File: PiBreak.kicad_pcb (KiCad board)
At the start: 2 copper layers, 56 x 62.9 mm, 317 parts, among them P1 RASPBERRY_PI_P1, P2 CONN_17, P3 CONN_8, P4 CONN_8, P5 CONN_8

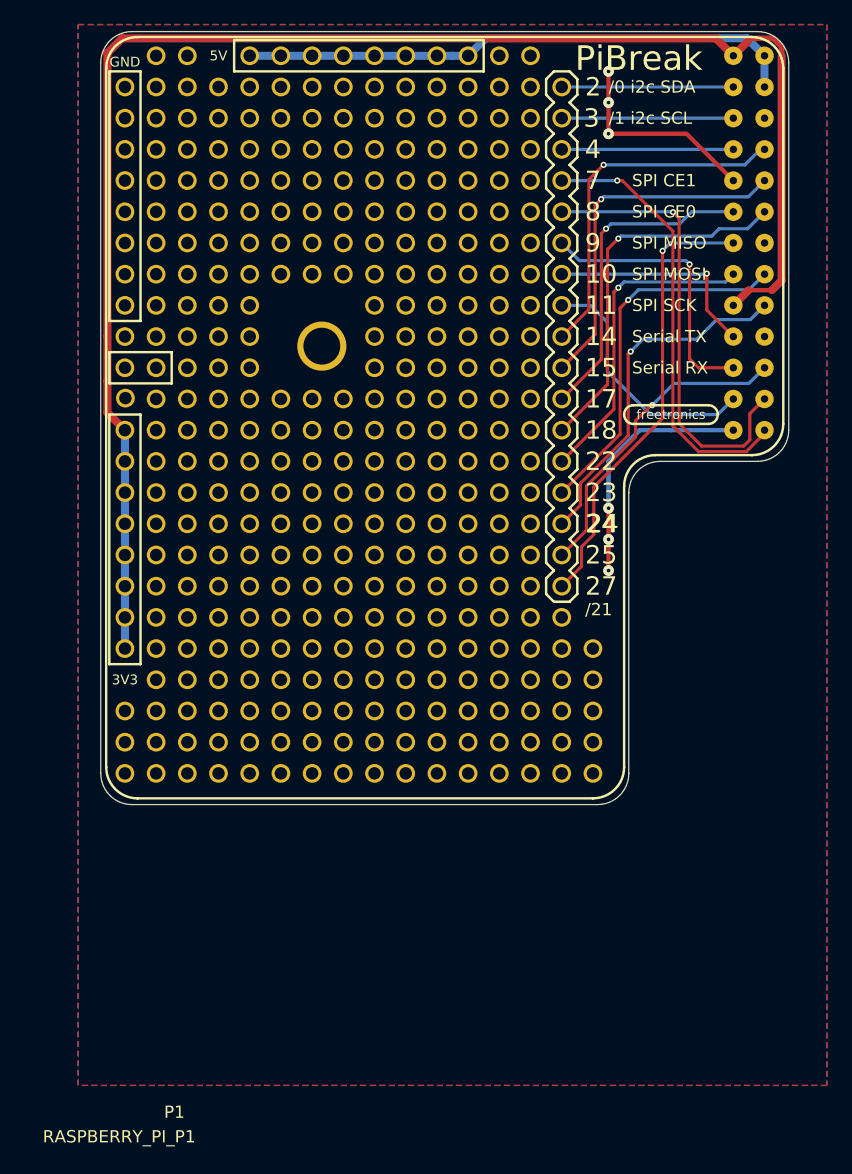
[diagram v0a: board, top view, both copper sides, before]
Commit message: Fix pad size for P1 header (was marginally too small)
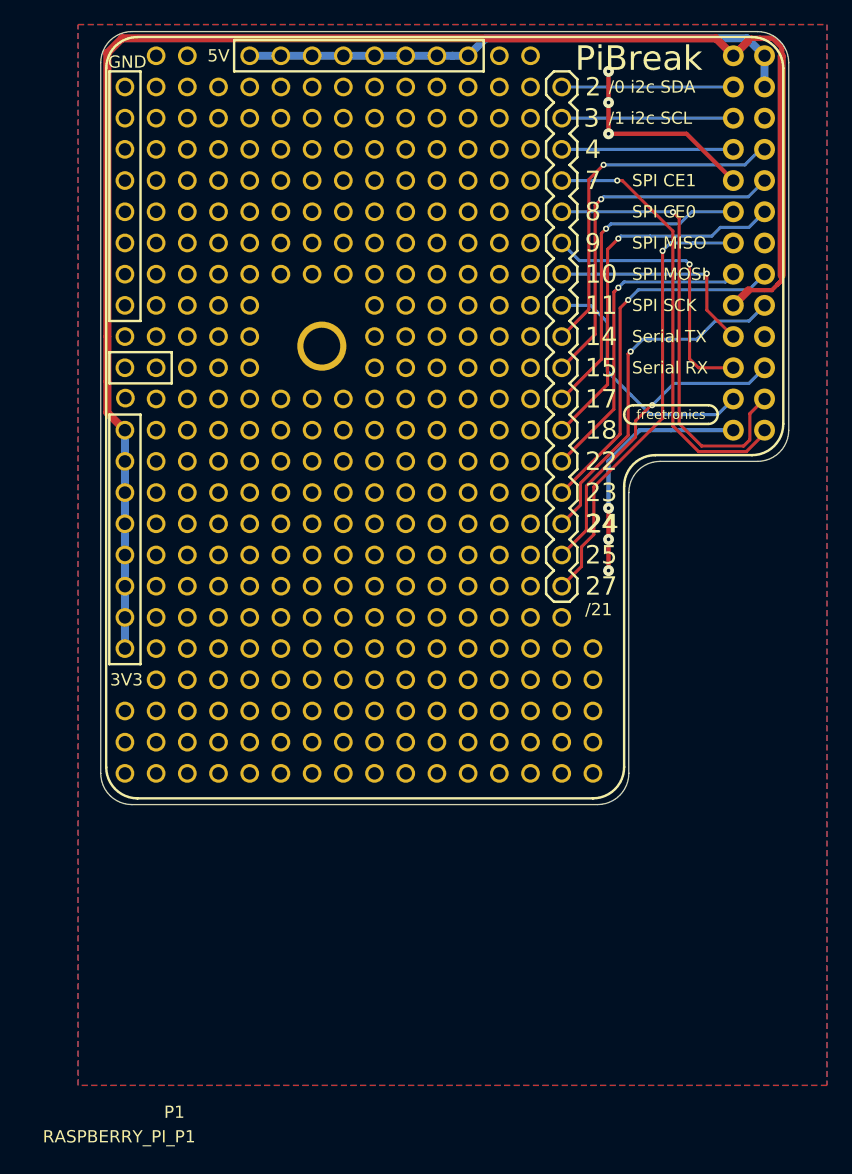
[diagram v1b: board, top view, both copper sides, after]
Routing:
- net +3.3V: track 131.8 -> 132.3 mm
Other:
- board text added: "V0.3 SKU: PIBR"
- board text removed: "V0.2 SKU: PIBR"

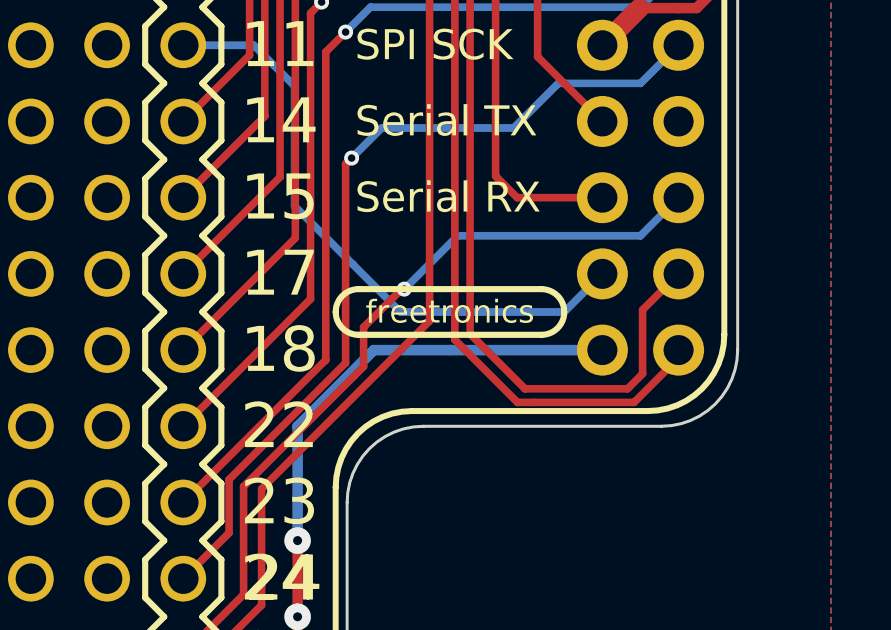
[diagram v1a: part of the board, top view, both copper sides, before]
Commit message: Label PWM pin GPIO 18
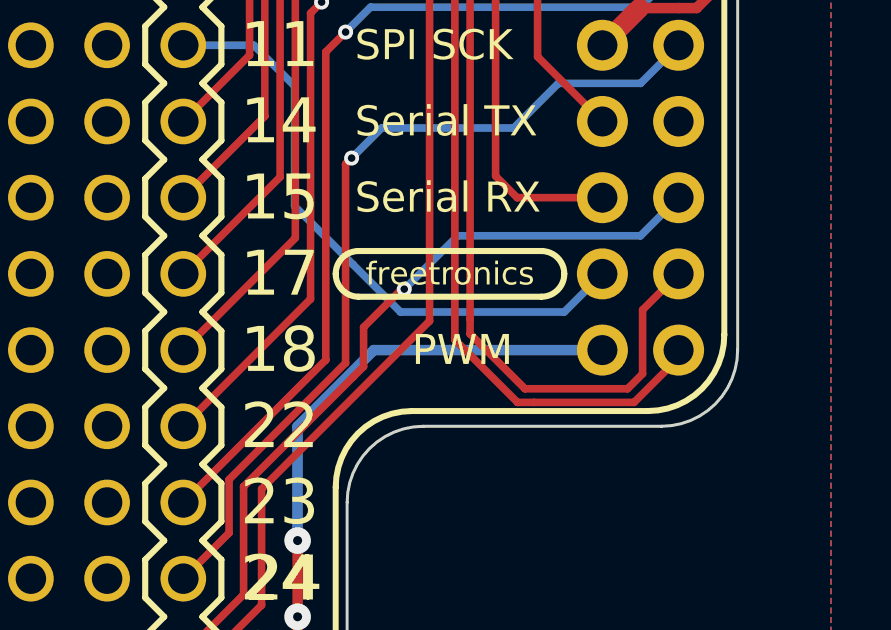
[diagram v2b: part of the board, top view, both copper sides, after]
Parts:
- moved LOGO_FREETRONICS_SMALL 1.27 mm to (259.1, 124.5)
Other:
- board text added: "PWM"
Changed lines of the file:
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@@
     (area 205.551667 93.98 274.144643 185.295)
     (thickness 1.6)
-    (drawings 220)
+    (drawings 221)
     (tracks 190)
     (zones 0)
@@
     (18 B.Paste user)
     (19 F.Paste user)
-    (20 B.SilkS user)
+    (20 B.SilkS user hide)
     (21 F.SilkS user)
     (22 B.Mask user)
@@
   )
   (module LOGO_FREETRONICS_SMALL (layer F.Cu)
-    (at 259.08 125.73)
+    (at 259.08 124.46)
     (fp_text reference LOGO_FREETRONICS_SMALL (at -0.508 0) (layer F.SilkS) hide
       (effects (font (size 0.127 0.127) (thickness 0.03175)))
@@
     )
   )
+  (gr_text PWM (at 257.81 127) (layer F.SilkS)
+    (effects (font (size 1 1) (thickness 0.2)) (justify left))
+  )
   (gr_text 3V3 (at 214.6935 147.32) (layer B.SilkS)

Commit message: Add v1.0 to silkscreen
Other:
- board text added: "V1.0 SKU: PIBR"
- board text removed: "V0.3 SKU: PIBR"
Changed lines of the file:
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@@
     (18 B.Paste user)
     (19 F.Paste user)
-    (20 B.SilkS user hide)
+    (20 B.SilkS user)
     (21 F.SilkS user)
     (22 B.Mask user)
@@
     (effects (font (size 1.5 1.5) (thickness 0.375)) (justify mirror))
   )
-  (gr_text "V0.3 SKU: PIBR" (at 257.048 117.348 90) (layer B.SilkS)
+  (gr_text "V1.0 SKU: PIBR" (at 257.048 117.348 90) (layer B.SilkS)
     (effects (font (size 1.2 1.2) (thickness 0.3)) (justify mirror))
   )
